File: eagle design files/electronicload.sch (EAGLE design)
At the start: 31 parts, among them Q1 IRLB3034PbF, U1 ARDUINO_BLUEPILL, U2 LMV324, X1 ED350/2

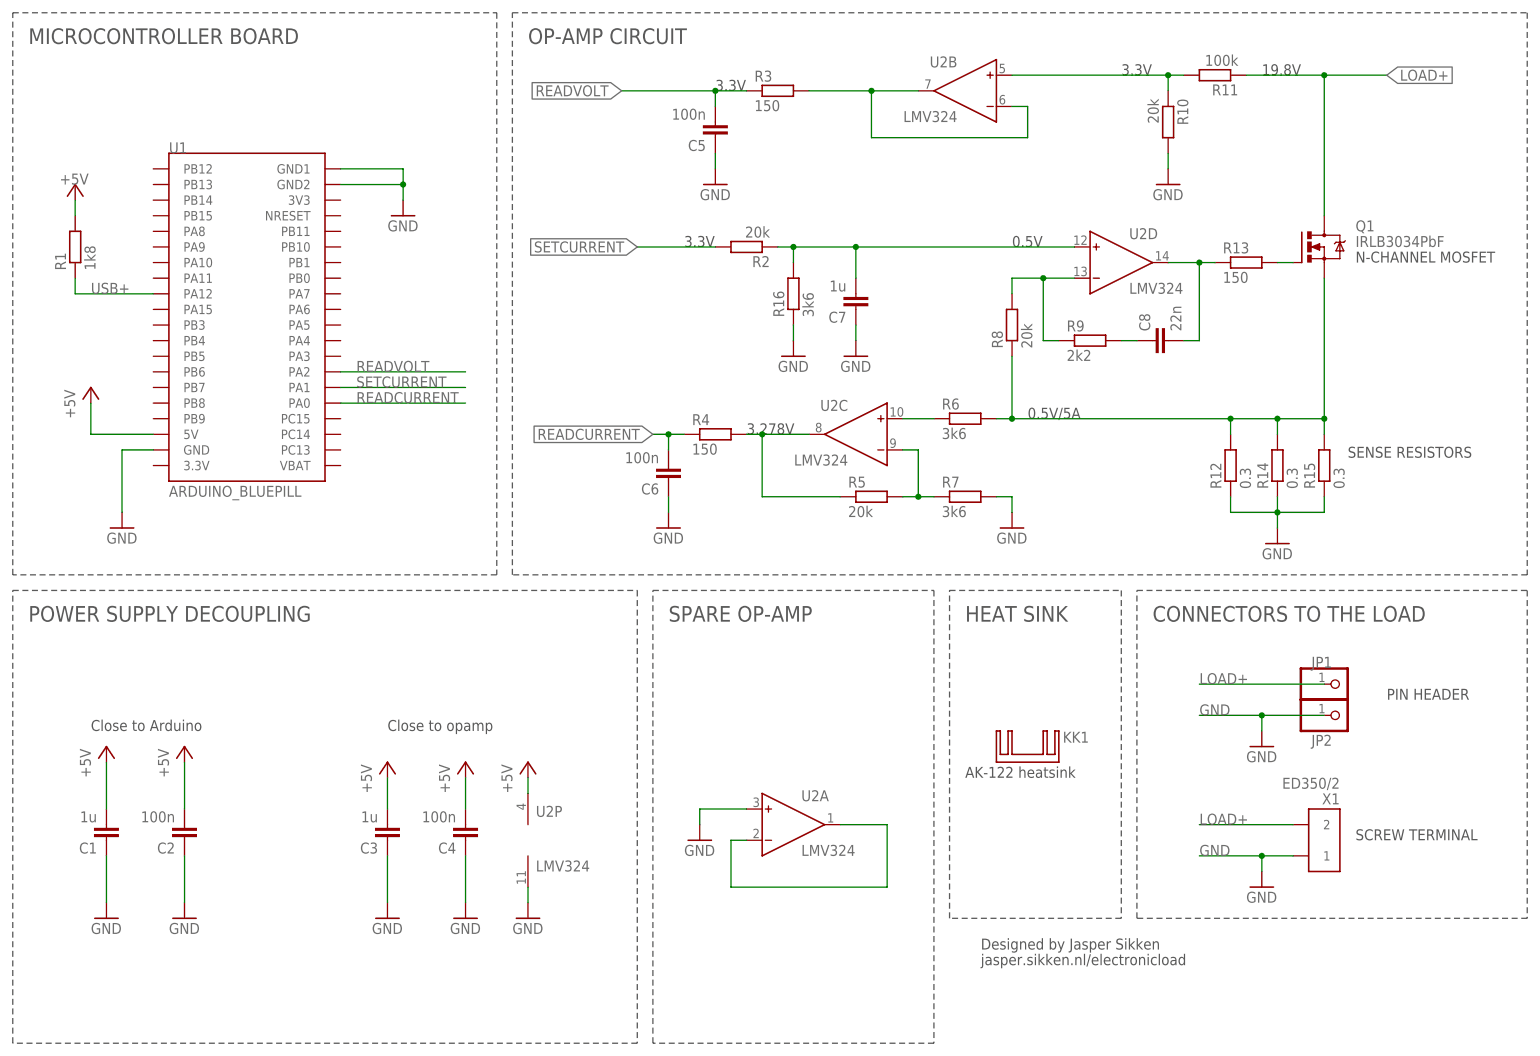
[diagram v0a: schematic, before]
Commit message: R2.01 Changed capacitor values.
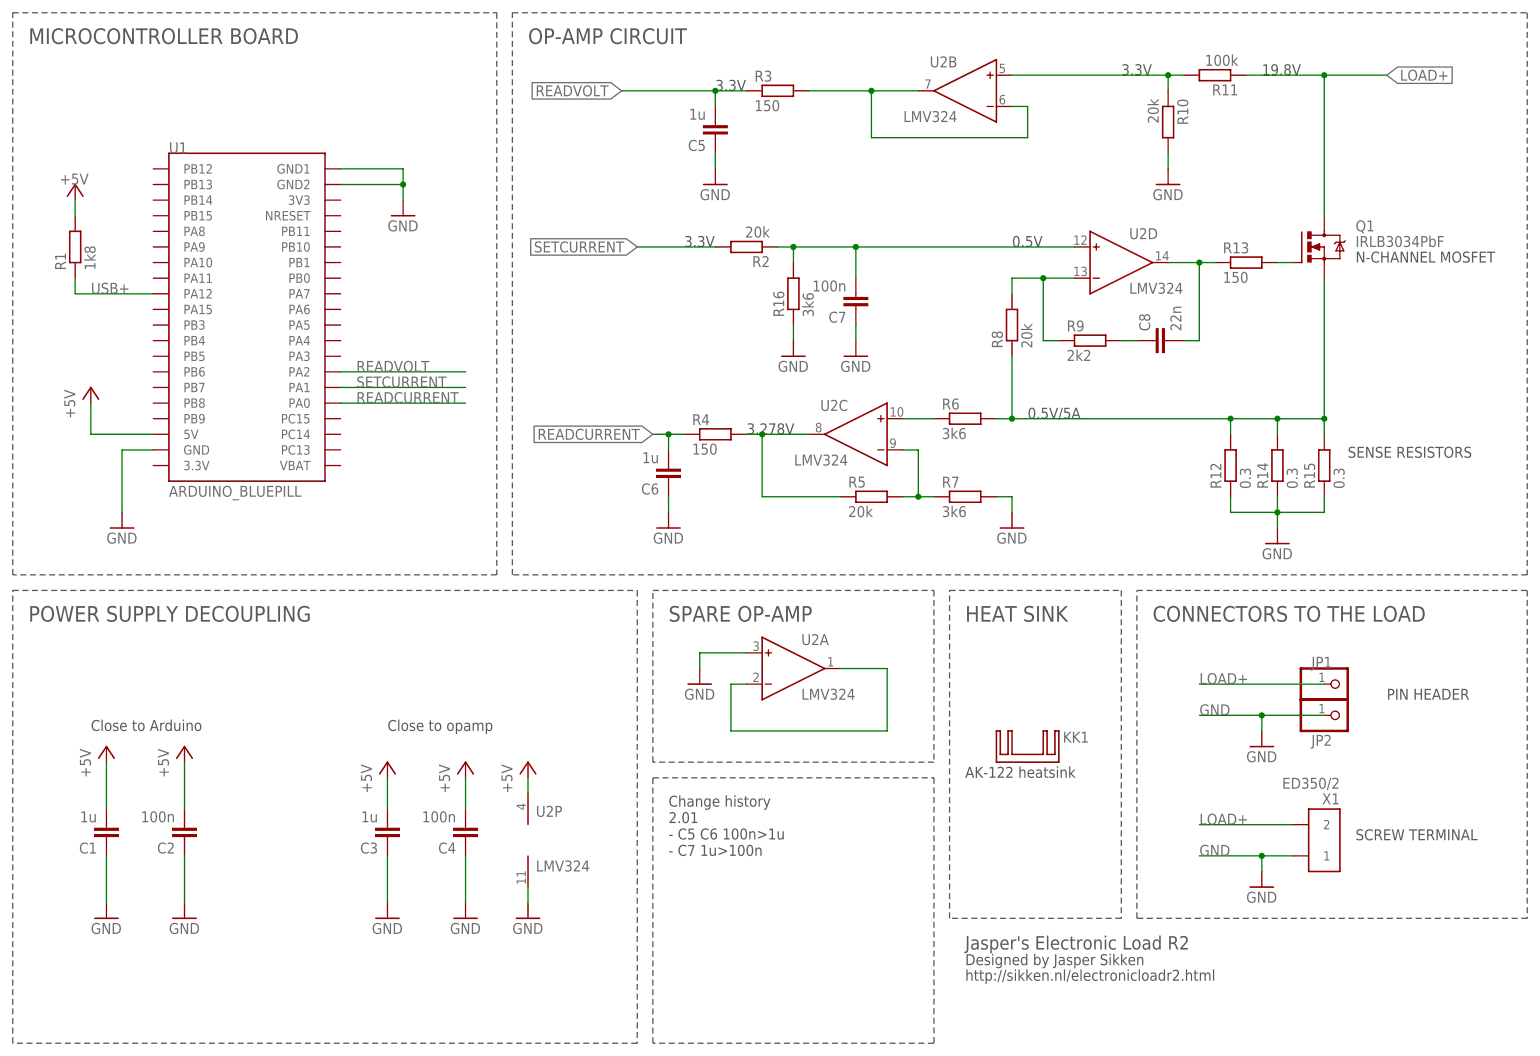
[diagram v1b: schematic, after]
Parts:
- C5, C6: value 100n -> 1u
- C7: value 1u -> 100n
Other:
- note added: "Change history 2.01 - C5 C6 100n>1u - C7 1u>100n"
- note added: "Jasper's Electronic Load R2"
- note added: "http://sikken.nl/electronicloadr2.html"
- note removed: "jasper.sikken.nl/electronicload"
- moved on the sheet: U2A
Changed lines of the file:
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@@
 <attribute name="DIGIKEY" value="IRLB3034PbF"/>
 </part>
-<part name="C5" library="rcl" library_urn="urn:adsk.eagle:library:334" deviceset="C-EU" device="C0603K" package3d_urn="urn:adsk.eagle:package:23680/2" value="100n">
+<part name="C5" library="rcl" library_urn="urn:adsk.eagle:library:334" deviceset="C-EU" device="C0603K" package3d_urn="urn:adsk.eagle:package:23680/2" value="1u">
 <attribute name="DIGIKEY" value="445-7456-1-ND"/>
 <attribute name="TEMPCOEFF" value="X5R"/>
@@
 <attribute name="VOLTAGE" value="50V"/>
 </part>
-<part name="C7" library="rcl" library_urn="urn:adsk.eagle:library:334" deviceset="C-EU" device="C0603K" package3d_urn="urn:adsk.eagle:package:23680/2" value="1u">
+<part name="C7" library="rcl" library_urn="urn:adsk.eagle:library:334" deviceset="C-EU" device="C0603K" package3d_urn="urn:adsk.eagle:package:23680/2" value="100n">
 <attribute name="DIGIKEY" value="445-12511-1-ND"/>
 <attribute name="TEMPCOEFF" value="X5R"/>
@@
 <attribute name="VOLTAGE" value="50V"/>
 </part>
-<part name="C6" library="rcl" library_urn="urn:adsk.eagle:library:334" deviceset="C-EU" device="C0603K" package3d_urn="urn:adsk.eagle:package:23680/2" value="100n">
+<part name="C6" library="rcl" library_urn="urn:adsk.eagle:library:334" deviceset="C-EU" device="C0603K" package3d_urn="urn:adsk.eagle:package:23680/2" value="1u">
 <attribute name="DIGIKEY" value="445-7456-1-ND"/>
 <attribute name="TEMPCOEFF" value="X5R"/>
@@
 <text x="127" y="104.14" size="1.778" layer="97">3.278V</text>
 <text x="121.92" y="160.02" size="1.778" layer="97">3.3V</text>
-<text x="165.1" y="20.32" size="1.778" layer="97">Designed by Jasper Sikken</text>
-<text x="165.1" y="17.78" size="1.778" layer="97">jasper.sikken.nl/electronicload</text>
+<text x="162.56" y="17.78" size="1.778" layer="97">Designed by Jasper Sikken</text>
+<text x="162.56" y="15.24" size="1.778" layer="97">http://sikken.nl/electronicloadr2.html</text>
 <text x="20.32" y="55.88" size="1.778" layer="97">Close to Arduino</text>
 <text x="68.58" y="55.88" size="1.778" layer="97">Close to opamp</text>
@@
 <wire x1="7.62" y1="5.08" x2="7.62" y2="78.74" width="0.1524" layer="97" style="shortdash"/>
 <wire x1="111.76" y1="78.74" x2="157.48" y2="78.74" width="0.1524" layer="97" style="shortdash"/>
-<wire x1="157.48" y1="78.74" x2="157.48" y2="5.08" width="0.1524" layer="97" style="shortdash"/>
-<wire x1="157.48" y1="5.08" x2="111.76" y2="5.08" width="0.1524" layer="97" style="shortdash"/>
-<wire x1="111.76" y1="5.08" x2="111.76" y2="78.74" width="0.1524" layer="97" style="shortdash"/>
+<wire x1="157.48" y1="78.74" x2="157.48" y2="50.8" width="0.1524" layer="97" style="shortdash"/>
+<wire x1="157.48" y1="50.8" x2="111.76" y2="50.8" width="0.1524" layer="97" style="shortdash"/>
+<wire x1="111.76" y1="50.8" x2="111.76" y2="78.74" width="0.1524" layer="97" style="shortdash"/>
 <wire x1="160.02" y1="78.74" x2="187.96" y2="78.74" width="0.1524" layer="97" style="shortdash"/>
 <wire x1="187.96" y1="78.74" x2="187.96" y2="25.4" width="0.1524" layer="97" style="shortdash"/>
@@
 <text x="91.44" y="167.64" size="2.54" layer="97">OP-AMP CIRCUIT</text>
 <text x="162.56" y="48.26" size="1.778" layer="97">AK-122 heatsink</text>
+<text x="162.56" y="20.32" size="2.1844" layer="97">Jasper's Electronic Load R2</text>
+<text x="114.3" y="35.56" size="1.778" layer="97">Change history
+2.01
+- C5 C6 100n&gt;1u
+- C7 1u&gt;100n</text>
+<wire x1="111.76" y1="48.26" x2="157.48" y2="48.26" width="0.1524" layer="97" style="shortdash"/>
+<wire x1="157.48" y1="48.26" x2="157.48" y2="5.08" width="0.1524" layer="97" style="shortdash"/>
+<wire x1="157.48" y1="5.08" x2="111.76" y2="5.08" width="0.1524" layer="97" style="shortdash"/>
+<wire x1="111.76" y1="5.08" x2="111.76" y2="48.26" width="0.1524" layer="97" style="shortdash"/>
 </plain>
 <instances>
@@
 <attribute name="DIGIKEY" x="195.58" y="154.94" size="1.778" layer="96" rot="R270" display="off"/>
 </instance>
-<instance part="U2" gate="A" x="132.08" y="40.64"/>
+<instance part="U2" gate="A" x="132.08" y="66.04"/>
 <instance part="U2" gate="B" x="165.1" y="160.02" rot="MR0"/>
 <instance part="U2" gate="C" x="147.32" y="104.14" rot="MR0"/>
@@
 </instance>
 <instance part="P+7" gate="1" x="91.44" y="50.8"/>
-<instance part="GND8" gate="1" x="119.38" y="38.1"/>
+<instance part="GND8" gate="1" x="119.38" y="63.5"/>
 <instance part="GND11" gate="1" x="144.78" y="116.84"/>
 <instance part="C2" gate="G$1" x="35.56" y="38.1" smashed="yes" rot="R180">
@@
 <segment>
 <pinref part="GND8" gate="1" pin="GND"/>
-<wire x1="119.38" y1="40.64" x2="119.38" y2="43.18" width="0.1524" layer="91"/>
+<wire x1="119.38" y1="66.04" x2="119.38" y2="68.58" width="0.1524" layer="91"/>
 <pinref part="U2" gate="A" pin="IN+"/>
-<wire x1="119.38" y1="43.18" x2="127" y2="43.18" width="0.1524" layer="91"/>
+<wire x1="119.38" y1="68.58" x2="127" y2="68.58" width="0.1524" layer="91"/>
 </segment>
 <segment>
@@
 <net name="N$20" class="0">
 <segment>
-<wire x1="149.86" y1="30.48" x2="149.86" y2="40.64" width="0.1524" layer="91"/>
-<wire x1="124.46" y1="30.48" x2="149.86" y2="30.48" width="0.1524" layer="91"/>
-<wire x1="124.46" y1="38.1" x2="124.46" y2="30.48" width="0.1524" layer="91"/>
+<wire x1="149.86" y1="55.88" x2="149.86" y2="66.04" width="0.1524" layer="91"/>
+<wire x1="124.46" y1="55.88" x2="149.86" y2="55.88" width="0.1524" layer="91"/>
+<wire x1="124.46" y1="63.5" x2="124.46" y2="55.88" width="0.1524" layer="91"/>
 <pinref part="U2" gate="A" pin="IN-"/>
-<wire x1="124.46" y1="38.1" x2="127" y2="38.1" width="0.1524" layer="91"/>
+<wire x1="124.46" y1="63.5" x2="127" y2="63.5" width="0.1524" layer="91"/>
 <pinref part="U2" gate="A" pin="OUT"/>
-<wire x1="142.24" y1="40.64" x2="149.86" y2="40.64" width="0.1524" layer="91"/>
+<wire x1="142.24" y1="66.04" x2="149.86" y2="66.04" width="0.1524" layer="91"/>
 </segment>
 </net>
@@
 </drawing>
 <compatibility>
+<note version="6.3" minversion="6.2.2" severity="warning">
+Since Version 6.2.2 text objects can contain more than one line,
+which will not be processed correctly with this version.
+</note>
 <note version="8.2" severity="warning">
 Since Version 8.2, EAGLE supports online libraries. The ids

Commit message: R2.02 changed opamp to MCP6004-I/SL
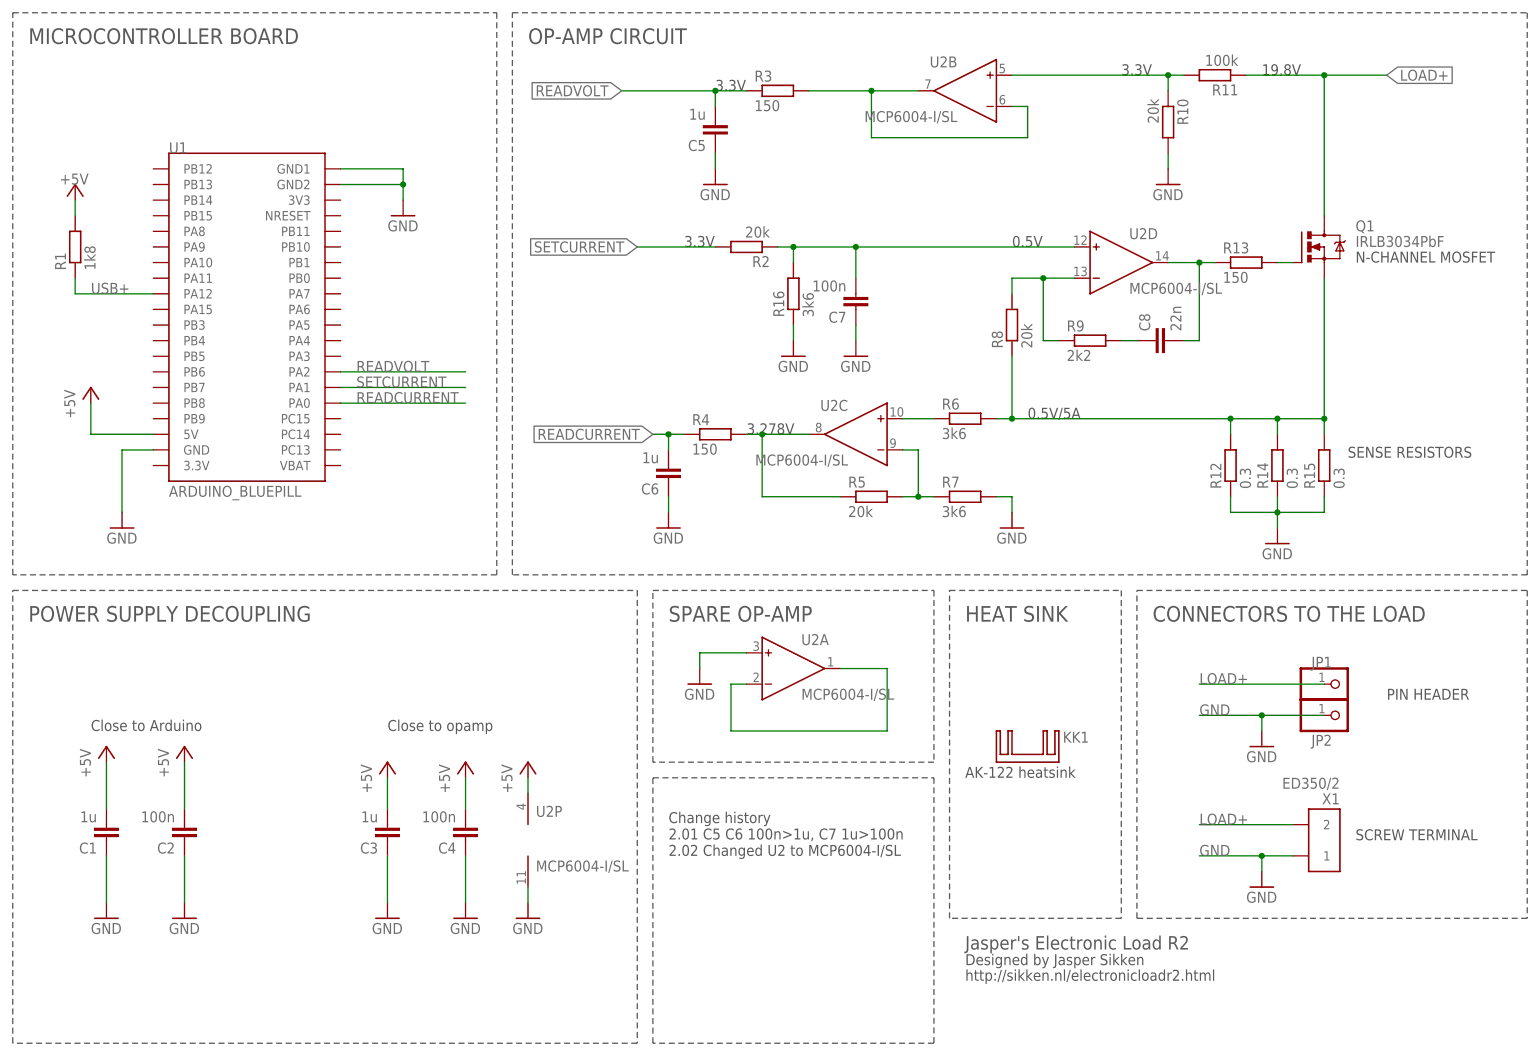
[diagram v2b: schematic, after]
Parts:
- U2: value LMV324 -> MCP6004-I/SL
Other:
- note added: "Change history 2.01 C5 C6 100n>1u, C7 1u>100n 2.02 Changed U2 to MCP6004-I/SL"
- note removed: "Change history 2.01 - C5 C6 100n>1u - C7 1u>100n"
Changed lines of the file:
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@@
 <?xml version="1.0" encoding="utf-8"?>
 <!DOCTYPE eagle SYSTEM "eagle.dtd">
-<eagle version="8.3.2">
+<eagle version="8.4.1">
 <drawing>
 <settings>
@@
 <attribute name="DIGIKEY" value="RMCF0603JT20K0CT-ND"/>
 </part>
-<part name="U2" library="electronicload" deviceset="AD8608" device="R" value="LMV324">
+<part name="U2" library="electronicload" deviceset="AD8608" device="R" value="MCP6004-I/SL">
 <attribute name="DIGIKEY" value=""/>
 </part>
@@
 <text x="162.56" y="20.32" size="2.1844" layer="97">Jasper's Electronic Load R2</text>
 <text x="114.3" y="35.56" size="1.778" layer="97">Change history
-2.01
-- C5 C6 100n&gt;1u
-- C7 1u&gt;100n</text>
+2.01 C5 C6 100n&gt;1u, C7 1u&gt;100n
+2.02 Changed U2 to MCP6004-I/SL</text>
 <wire x1="111.76" y1="48.26" x2="157.48" y2="48.26" width="0.1524" layer="97" style="shortdash"/>
 <wire x1="157.48" y1="48.26" x2="157.48" y2="5.08" width="0.1524" layer="97" style="shortdash"/>
